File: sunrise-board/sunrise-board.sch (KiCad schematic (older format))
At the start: 32 parts, among them J1 Barrel Jack 12V, J2 Header, J3 FTDI Basic, J4 Header, J5 LED_STRIP_VGRB, J6 I2C, Q1 IRLZ34N, Q2 IRLZ34N, Q3 IRLZ34N, SW1 Reset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

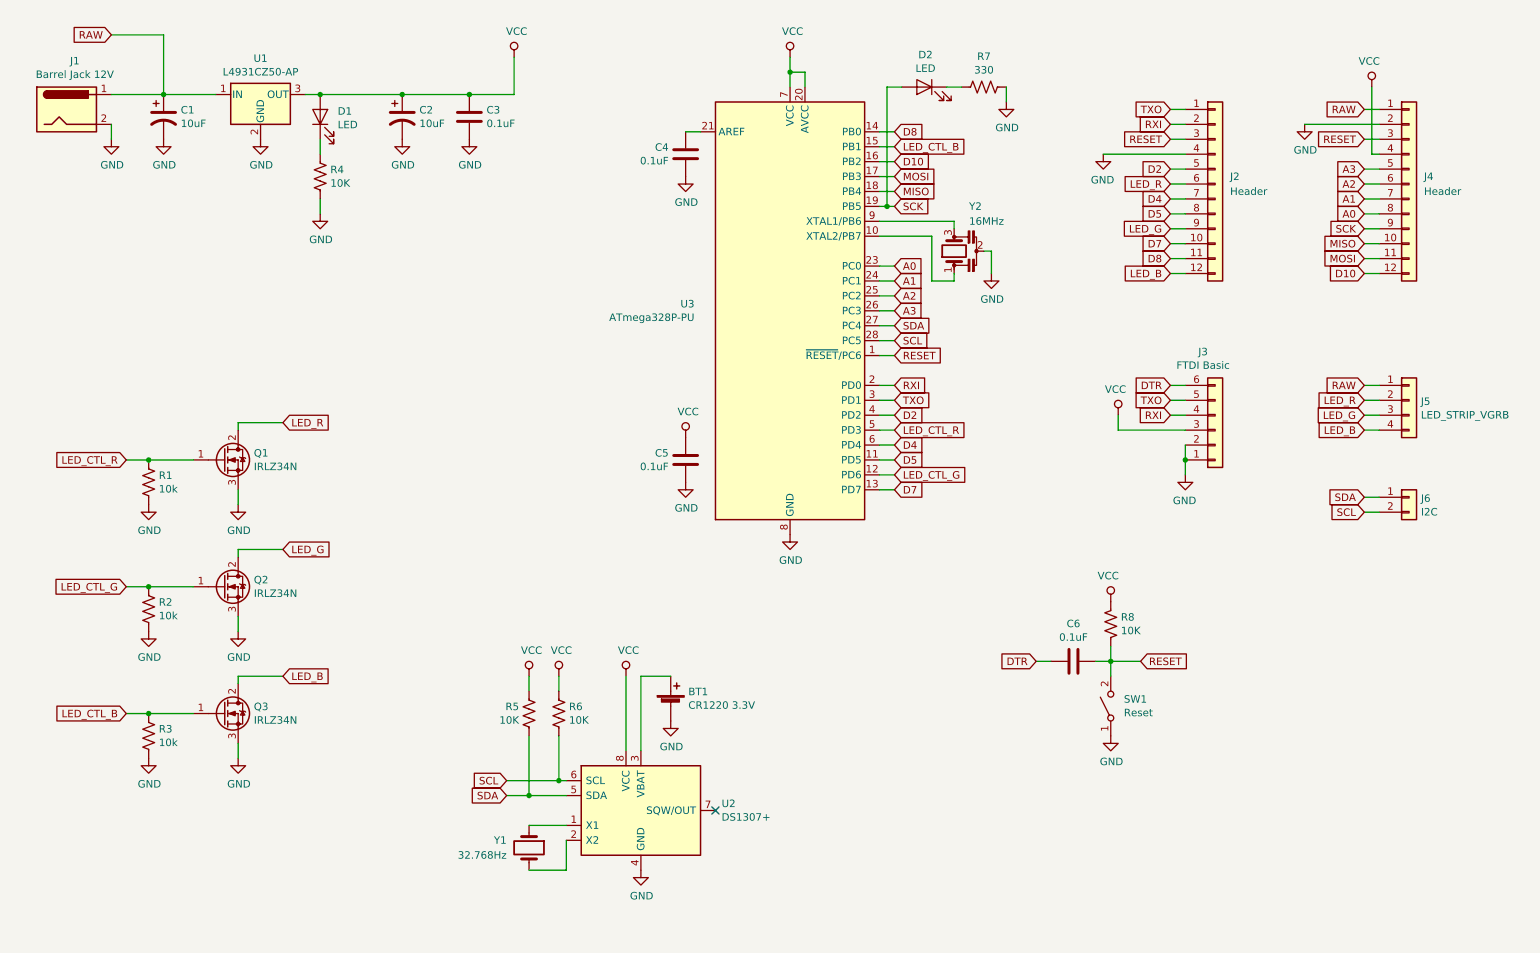
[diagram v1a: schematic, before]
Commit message: updates to silk screen
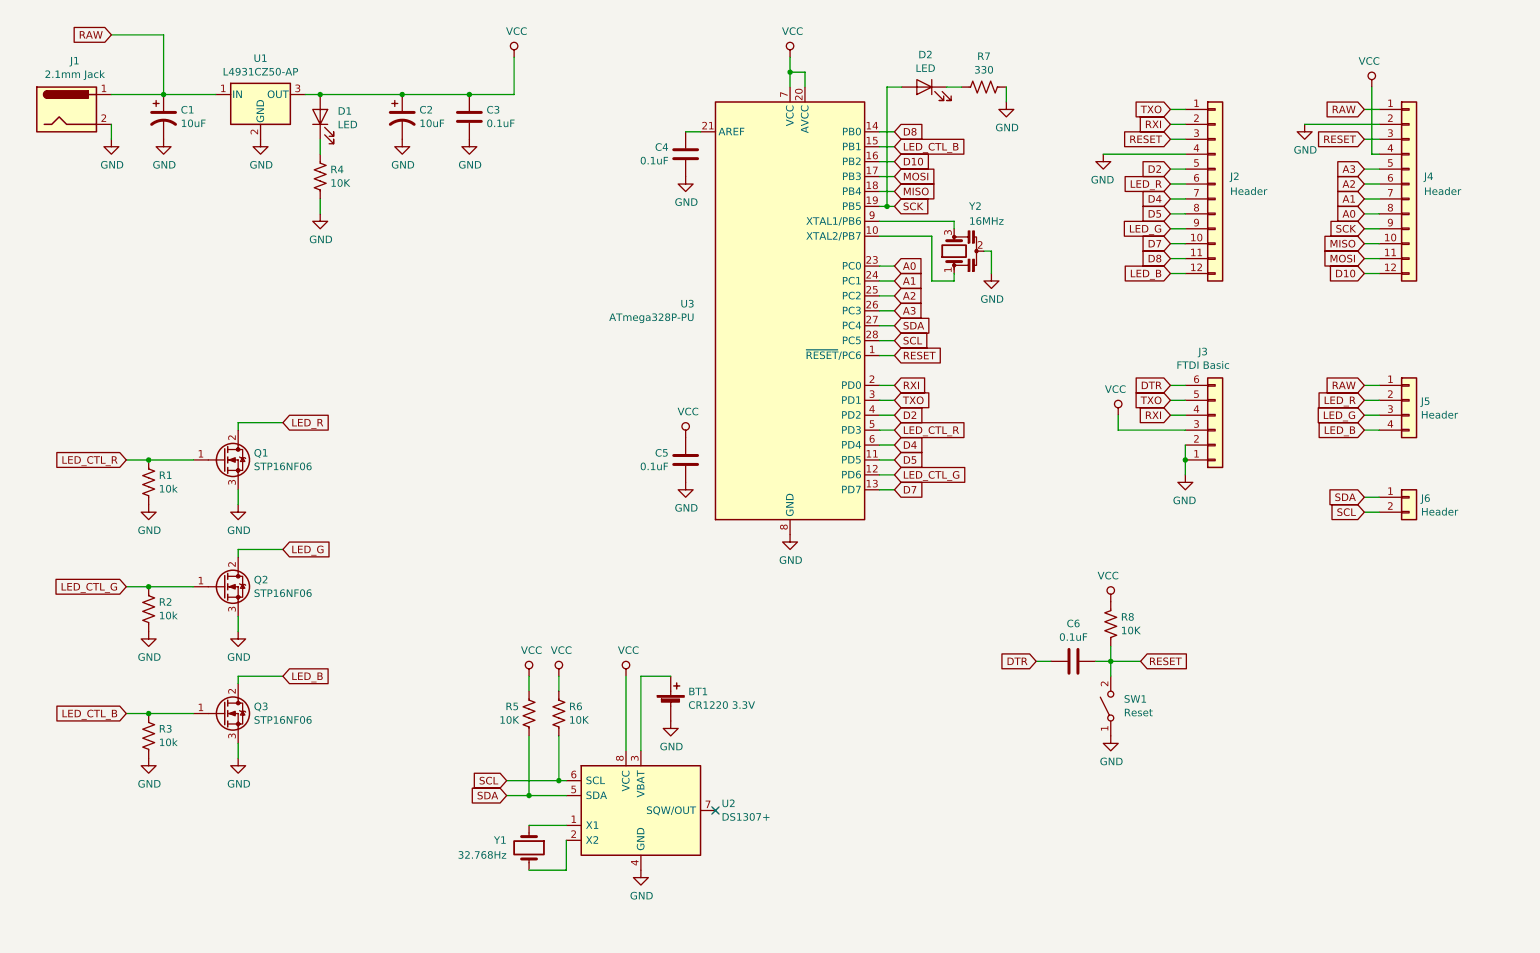
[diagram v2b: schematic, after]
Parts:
- BT1: Link (none) -> https://www.mouser.com/ProductDetail/712-BAT-HLD-012-THM
- J1: value Barrel Jack 12V -> 2.1mm Jack; Link (none) -> https://www.mouser.com/ProductDetail/PJ-102A
- J5: value LED_STRIP_VGRB -> Header
- J6: value I2C -> Header
- Q1, Q2, Q3: value IRLZ34N -> STP16NF06; Link (none) -> https://www.mouser.com/ProductDetail/STP16NF06
- SW1: Link (none) -> https://www.mouser.com/ProductDetail/SKHHAJA010
- U1: Link (none) -> https://www.mouser.com/ProductDetail/511-L4931CZ50-AP
- U2: Link (none) -> https://www.mouser.com/ProductDetail/700-DS1307
- U3: Link (none) -> https://www.mouser.com/ProductDetail/ATMEGA328P-PU
- Y1: Link (none) -> https://www.mouser.com/ProductDetail/449-LFXTAL002997BULK
- Y2: Link (none) -> https://www.mouser.com/ProductDetail/81-CSTLS16M0X55-A0
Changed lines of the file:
@@
 P 2400 4000
 F 0 "Q1" H 2605 4046 50  0000 L CNN
-F 1 "IRLZ34N" H 2605 3955 50  0000 L CNN
+F 1 "STP16NF06" H 2605 3955 50  0000 L CNN
 F 2 "Package_TO_SOT_THT:TO-220-3_Vertical" H 2650 3925 50  0001 L CIN
-F 3 "http://www.infineon.com/dgdl/irlz34npbf.pdf?fileId=5546d462533600a40153567206892720" H 2400 4000 50  0001 L CNN
+F 3 "https://www.st.com/resource/en/datasheet/cd00002501.pdf" H 2400 4000 50  0001 L CNN
+F 4 "https://www.mouser.com/ProductDetail/STP16NF06" H 0   0   50  0001 C CNN "Link"
 	1    2400 4000
 	1    0    0    -1
@@
 P 2400 4850
 F 0 "Q2" H 2605 4896 50  0000 L CNN
-F 1 "IRLZ34N" H 2605 4805 50  0000 L CNN
+F 1 "STP16NF06" H 2605 4805 50  0000 L CNN
 F 2 "Package_TO_SOT_THT:TO-220-3_Vertical" H 2650 4775 50  0001 L CIN
-F 3 "http://www.infineon.com/dgdl/irlz34npbf.pdf?fileId=5546d462533600a40153567206892720" H 2400 4850 50  0001 L CNN
+F 3 "https://www.st.com/resource/en/datasheet/cd00002501.pdf" H 2400 4850 50  0001 L CNN
+F 4 "https://www.mouser.com/ProductDetail/STP16NF06" H 0   0   50  0001 C CNN "Link"
 	1    2400 4850
 	1    0    0    -1
@@
 P 2400 5700
 F 0 "Q3" H 2605 5746 50  0000 L CNN
-F 1 "IRLZ34N" H 2605 5655 50  0000 L CNN
+F 1 "STP16NF06" H 2605 5655 50  0000 L CNN
 F 2 "Package_TO_SOT_THT:TO-220-3_Vertical" H 2650 5625 50  0001 L CIN
-F 3 "http://www.infineon.com/dgdl/irlz34npbf.pdf?fileId=5546d462533600a40153567206892720" H 2400 5700 50  0001 L CNN
+F 3 "https://www.st.com/resource/en/datasheet/cd00002501.pdf" H 2400 5700 50  0001 L CNN
+F 4 "https://www.mouser.com/ProductDetail/STP16NF06" H 0   0   50  0001 C CNN "Link"
 	1    2400 5700
 	1    0    0    -1
@@
 P 1350 1650
 F 0 "J1" H 1405 1975 50  0000 C CNN
-F 1 "Barrel Jack 12V" H 1405 1884 50  0000 C CNN
+F 1 "2.1mm Jack" H 1405 1884 50  0000 C CNN
 F 2 "Connector_BarrelJack:BarrelJack_Horizontal" H 1400 1610 50  0001 C CNN
-F 3 "~" H 1400 1610 50  0001 C CNN
+F 3 "https://www.cui.com/product/resource/pj-102a.pdf" H 1400 1610 50  0001 C CNN
+F 4 "https://www.mouser.com/ProductDetail/PJ-102A" H 0   0   50  0001 C CNN "Link"
 	1    1350 1650
 	1    0    0    -1
@@
 F 1 "ATmega328P-PU" H 5559 2955 50  0000 R CNN
 F 2 "Package_DIP:DIP-28_W7.62mm" H 6200 3000 50  0001 C CIN
-F 3 "http://ww1.microchip.com/downloads/en/DeviceDoc/ATmega328_P%20AVR%20MCU%20with%20picoPower%20Technology%20Data%20Sheet%2040001984A.pdf" H 6200 3000 50  0001 C CNN
+F 3 "http://ww1.microchip.com/downloads/en/DeviceDoc/ATmega48A-PA-88A-PA-168A-PA-328-P-DS-DS40002061A.pdf" H 6200 3000 50  0001 C CNN
+F 4 "https://www.mouser.com/ProductDetail/ATMEGA328P-PU" H 0   0   50  0001 C CNN "Link"
 	1    6200 3000
 	1    0    0    -1
@@
 F 2 "Package_DIP:DIP-8_W7.62mm" H 5200 5850 50  0001 C CNN
 F 3 "https://datasheets.maximintegrated.com/en/ds/DS1307.pdf" H 5200 6150 50  0001 C CNN
+F 4 "https://www.mouser.com/ProductDetail/700-DS1307" H 5200 6350 50  0001 C CNN "Link"
 	1    5200 6350
 	1    0    0    -1
@@
 F 1 "32.768Hz" V 4500 6450 50  0000 R CNN
 F 2 "Crystal:Crystal_C26-LF_D2.1mm_L6.5mm_Horizontal_1EP_style2" H 4450 6600 50  0001 C CNN
-F 3 "~" H 4450 6600 50  0001 C CNN
+F 3 "https://www.iqdfrequencyproducts.com/products/pn/LFXTAL002997Bulk.pdf" H 4450 6600 50  0001 C CNN
+F 4 "https://www.mouser.com/ProductDetail/449-LFXTAL002997BULK" H 0   0   50  0001 C CNN "Link"
 	1    4450 6600
 	0    1    1    0
@@
 F 1 "CR1220 3.3V" H 5518 5655 50  0000 L CNN
 F 2 "Sunrise:BatteryHolder_CR1220_THT" V 5400 5710 50  0001 C CNN
-F 3 "~" V 5400 5710 50  0001 C CNN
+F 3 "https://linxtechnologies.com/wp/wp-content/uploads/bat-hld-012-thm.pdf" V 5400 5710 50  0001 C CNN
+F 4 "https://www.mouser.com/ProductDetail/712-BAT-HLD-012-THM" H 0   0   50  0001 C CNN "Link"
 	1    5400 5650
 	1    0    0    -1
@@
 F 2 "Package_TO_SOT_THT:TO-92_Inline_Wide" H 2675 1400 50  0001 L CIN
 F 3 "https://www.st.com/resource/en/datasheet/l4931.pdf" H 2650 1500 50  0001 C CNN
+F 4 "https://www.mouser.com/ProductDetail/511-L4931CZ50-AP" H 0   0   50  0001 C CNN "Link"
 	1    2650 1550
 	1    0    0    -1
@@
 F 1 "Reset" V 8305 5562 50  0000 R CNN
 F 2 "Button_Switch_THT:SW_PUSH_6mm" H 8350 5650 50  0001 C CNN
-F 3 "" H 8350 5650 50  0001 C CNN
+F 3 "https://www.alps.com/prod/info/E/HTML/Tact/SnapIn/SKHH/SKHHAJA010.html" H 8350 5650 50  0001 C CNN
+F 4 "https://www.mouser.com/ProductDetail/SKHHAJA010" H 0   0   50  0001 C CNN "Link"
 	1    8350 5650
 	0    -1   -1   0
@@
 F 1 "16MHz" V 7500 2500 50  0000 R CNN
 F 2 "Crystal:Resonator-3Pin_W6.0mm_H3.0mm" H 7275 2600 50  0001 C CNN
-F 3 "~" H 7275 2600 50  0001 C CNN
+F 3 "https://www.murata.com/en-us/api/pdfdownloadapi?partno=CSTLS16M0X55-A0" H 7275 2600 50  0001 C CNN
+F 4 "https://www.mouser.com/ProductDetail/81-CSTLS16M0X55-A0" H 0   0   50  0001 C CNN "Link"
 	1    7300 2600
 	0    -1   -1   0
@@
 P 10350 3600
 F 0 "J5" H 10429 3592 50  0000 L CNN
-F 1 "LED_STRIP_VGRB" H 10429 3501 50  0000 L CNN
+F 1 "Header" H 10429 3501 50  0000 L CNN
 F 2 "Connector_PinHeader_2.54mm:PinHeader_1x04_P2.54mm_Vertical" H 10350 3600 50  0001 C CNN
 F 3 "~" H 10350 3600 50  0001 C CNN
@@
 P 10350 4250
 F 0 "J6" H 10430 4242 50  0000 L CNN
-F 1 "I2C" H 10430 4151 50  0000 L CNN
+F 1 "Header" H 10430 4151 50  0000 L CNN
 F 2 "Connector_PinHeader_2.54mm:PinHeader_1x02_P2.54mm_Vertical" H 10350 4250 50  0001 C CNN
 F 3 "~" H 10350 4250 50  0001 C CNN

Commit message: finish bom and docs
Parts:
- BT1: PartNumber (none) -> BAT-HLD-012-THM
- C1, C2: Link (none) -> https://www.mouser.com/ProductDetail/USR1E100MDD1TP; PartNumber (none) -> USR1E100MDD1TP
- C3, C4, C5, C6: Link (none) -> https://www.mouser.com/ProductDetail/K104K15X7RF53H5; PartNumber (none) -> K104K15X7RF53H5
- D1, D2: Link (none) -> https://www.mouser.com/ProductDetail/LTL-4222N; PartNumber (none) -> LTL-4222N
- J1: PartNumber (none) -> PJ-102A
- J3: Link (none) -> https://www.mouser.com/ProductDetail/TSW-106-08-T-S-RA; PartNumber (none) -> TSW-106-08-T-S-RA
- J5: Link (none) -> https://www.mouser.com/ProductDetail/TSW-130-07-T-S; PartNumber (none) -> TSW-130-07-T-S
- Q1, Q2, Q3: PartNumber (none) -> STP16NF06
- R1, R2, R3: Link (none) -> https://www.mouser.com/ProductDetail/CFR-25JT-52-10K; PartNumber (none) -> CFR-25JT-52-10K
- R4, R5, R6, R8: value 10K -> 10k; Link (none) -> https://www.mouser.com/ProductDetail/CFR-25JT-52-10K; PartNumber (none) -> CFR-25JT-52-10K
- R7: Link (none) -> https://www.mouser.com/ProductDetail/CFR-25JT-52-330R; PartNumber (none) -> CFR-25JT-52-330R
- SW1: PartNumber (none) -> SKHHAJA010
- U1: PartNumber (none) -> L4931CZ50-AP
- U2: PartNumber (none) -> DS1307+
- U3: PartNumber (none) -> ATMEGA328P-PU
- Y1: PartNumber (none) -> LFXTAL002997Bulk
- Y2: PartNumber (none) -> CSTLS16M0X55-A0
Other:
- moved on the sheet: BT1, R5, R6, U2, Y1

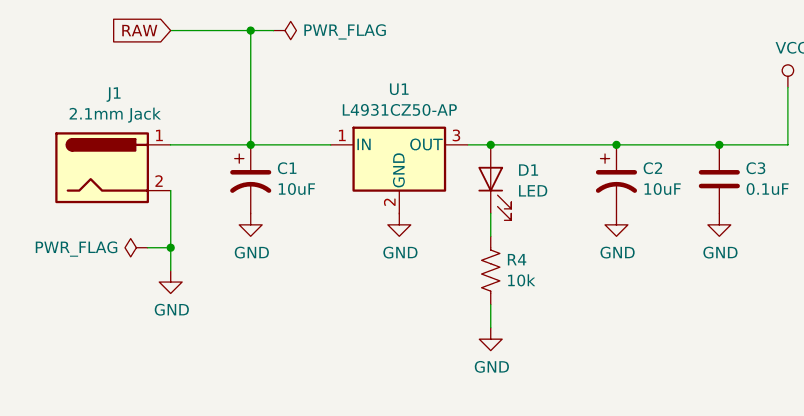
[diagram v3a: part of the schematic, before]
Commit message: fix voltage regulator pins
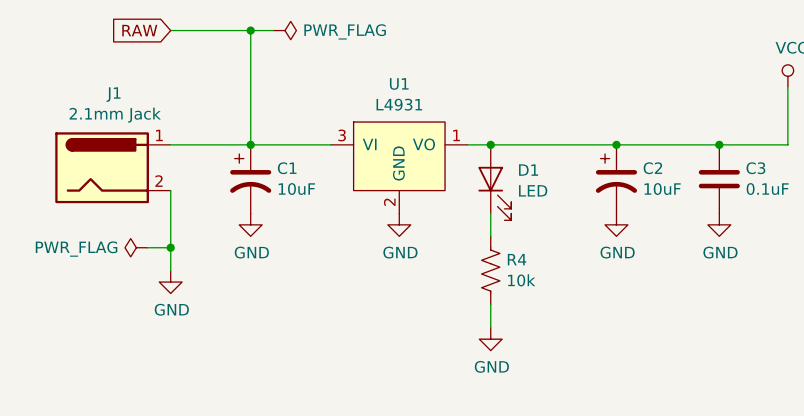
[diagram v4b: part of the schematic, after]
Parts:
- removed U1: L4931CZ50-AP, Package_TO_SOT_THT:TO-92_Inline_Wide, symbol Regulator_Linear:uA7805
- added U1: L4931, Package_TO_SOT_THT:TO-92_Inline_Wide, symbol sunrise:L4931
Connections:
- net GND: now also U1.2 (GND)
- net RAW: now also U1.3 (VI)
- net VCC: now also U1.1 (VO)
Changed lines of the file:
@@
 Sheet 1 1
 Title "Sunrise Alarm"
-Date "2019-06-04"
-Rev "v1"
+Date "2019-06-24"
+Rev "v2"
 Comp ""
 Comment1 "Arduino Mini and Arduino Pro Mini design by Team Arduino and Spark Fun Electronics"
-Comment2 "creativecommons.org/licenses/by-nc-sa/4.0"
-Comment3 "Licence: CC BY-NC-SA"
+Comment2 "Licence: CC BY-NC-SA"
+Comment3 "Source: github.com/tyehle/sunrise"
 Comment4 "Author: Tobin Yehle"
 $EndDescr
@@
 	2000 1550 2000 1050
 Connection ~ 2000 1550
-$Comp
-L Regulator_Linear:uA7805 U1
-U 1 1 5CF45A5F
-P 2650 1550
-F 0 "U1" H 2650 1792 50  0000 C CNN
-F 1 "L4931CZ50-AP" H 2650 1701 50  0000 C CNN
-F 2 "Package_TO_SOT_THT:TO-92_Inline_Wide" H 2675 1400 50  0001 L CIN
-F 3 "https://www.st.com/resource/en/datasheet/l4931.pdf" H 2650 1500 50  0001 C CNN
-F 4 "https://www.mouser.com/ProductDetail/511-L4931CZ50-AP" H 0   0   50  0001 C CNN "Link"
-F 5 "L4931CZ50-AP" H 0   0   50  0001 C CNN "PartNumber"
-	1    2650 1550
-	1    0    0    -1
-$EndComp
 Wire Wire Line
 	2350 1550 2000 1550
@@
 Wire Wire Line
 	5200 6050 5500 6050
+$Comp
+L sunrise:L4931 U1
+U 1 1 5D1308ED
+P 2650 1550
+F 0 "U1" H 2650 1815 50  0000 C CNN
+F 1 "L4931" H 2650 1724 50  0000 C CNN
+F 2 "Package_TO_SOT_THT:TO-92_Inline_Wide" H 2650 1550 50  0001 C CNN
+F 3 "https://www.st.com/resource/en/datasheet/l4931.pdf" H 2650 1550 50  0001 C CNN
+F 4 "https://www.mouser.com/ProductDetail/511-L4931CZ50-AP" H -700 350 50  0001 C CNN "Link"
+F 5 "L4931CZ50-AP" H -700 350 50  0001 C CNN "PartNumber"
+	1    2650 1550
+	1    0    0    -1
+$EndComp
 $EndSCHEMATC
